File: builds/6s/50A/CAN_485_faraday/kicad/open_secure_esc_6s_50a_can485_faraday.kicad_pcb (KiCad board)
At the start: 4 copper layers, 32 x 66.1 mm, 59 parts, among them J1 SolderPad_1x04_SMD_P1.27mm_Pr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, J2 SolderPad_1x02_SMD_P2.54mm, J3 SolderPad_1x02_SMD_P2.54mm, J4A SolderWirePad_1x01_SMD_5x10mm, J4B SolderWirePad_1x01_SMD_5x10mm, J4C SolderWirePad_1x01_SMD_5x10mm, J5A SolderWire-6sqmm_1x01_D3.5mm_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, J5B SolderWire-6sqmm_1x01_D3.5mm_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, Q1 Toshiba_2-5W1A_SOP-Advance-N_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, Q2 Toshiba_2-5W1A_SOP-Advance-N_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, Q3 Toshiba_2-5W1A_SOP-Advance-N_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, Q4 Toshiba_2-5W1A_SOP-Advance-N_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, Q5 Toshiba_2-5W1A_SOP-Advance-N_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, Q6 Toshiba_2-5W1A_SOP-Advance-N_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, U1 LQFP-64_10x10mm_P0.5mm, U2 Infineon_PG-USON-10-2-4_3x3mm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, U3 SOIC-20W_7.5x12.8mm_P1.27mm, U4 SOIC-20W_7.5x12.8mm_P1.27mm, U5 TI_RTA0040B_WQFN-40_6x6mm_P0.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, U6 SOIC-8_3.9x4.9mm_P1.27mm, U7 SOIC-8_3.9x4.9mm_P1.27mm, U8 SOIC-8_3.9x4.9mm_P1.27mm

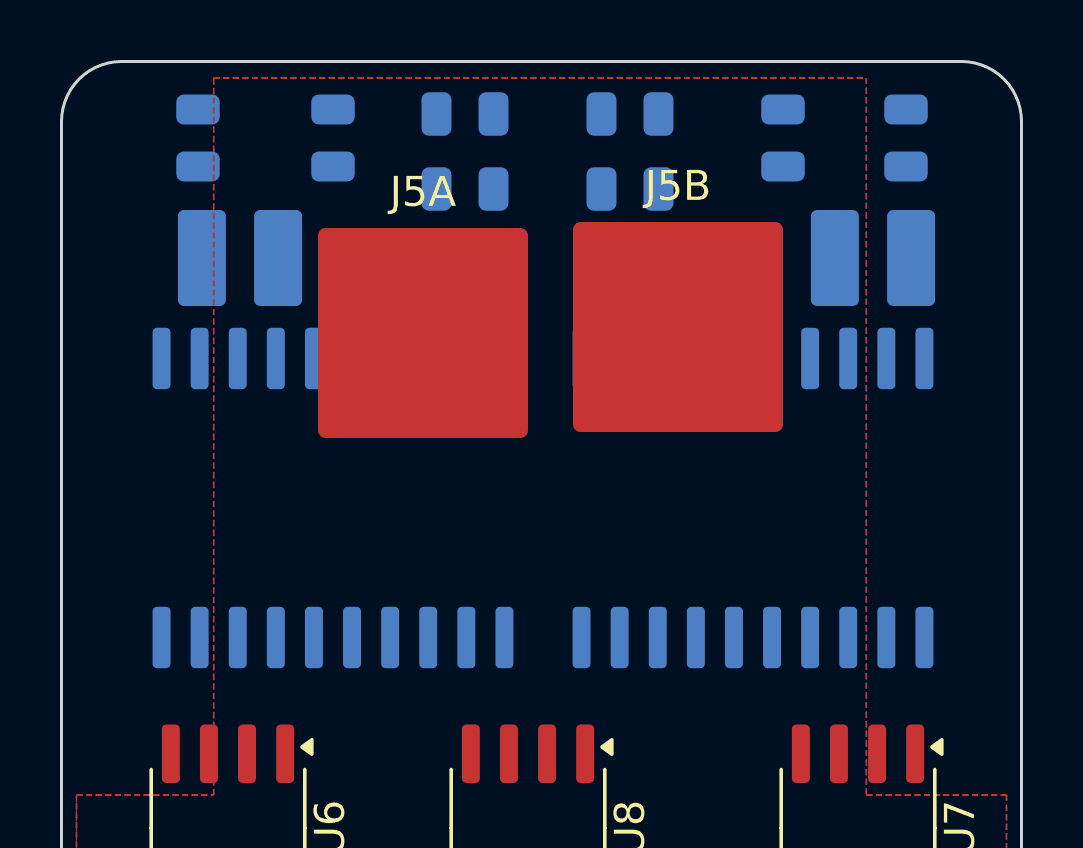
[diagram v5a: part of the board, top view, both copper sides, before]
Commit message: Creepage 7.51 -> 7.98 mm: the ceiling was my formula, not the board
The repo owner pushed back on two assertions and both were wrong.

FIRST: I claimed the FET columns could not move inboard because SH1's land is
a fixed 22.20 mm and they must sit within it. They already overhang it --
Q1/Q2 by 0.75 mm, Q5/Q6 by 2.75 mm -- with 5.30 and 6.30 mm of slack between
columns. The claim was asserted without checking.

SECOND, AND THE REAL ONE: edge_path() computed insetA + thickness + insetB,
which silently assumes two opposite-face parts sit at the same position ALONG
the edge. They rarely do. The true creepage path is the unfolded surface
distance,

    sqrt( along_edge_separation^2 + (insetA + thickness + insetB)^2 )

U3 against Q2 are ~26 mm apart in y, so the real path is 27.15 mm where the
harness was reporting 7.83. Every opposite-face pair was being scored as
though it sat directly across the edge.

With that corrected the picture inverts. The FETs stop being binders
entirely -- every around-edge pair is 7.98 mm or better -- and the only real
constraint is the in-plane U3.20 <-> U4.10 pair, which is exactly what
spreading the transceivers apart relieves. Sweeping it:

    spread +/-0.0  creepage 7.51  DRC 0
    spread +/-0.5  creepage 7.83  DRC 0
    spread +/-1.0  creepage 7.98  DRC 0   <- applied
    spread +/-2.0  creepage 7.98  DRC 0
    spread +/-2.5  creepage 7.98  DRC 4

Applied +/-1.0 mm. Creepage 7.98 with 0.48 mm of margin instead of 0.01,
DRC electrical 0, isolated lead unchanged at 9.76 mm, both isolation rules
still passing. No board resize needed.

This is the third harness bug found by checking it against geometry rather
than trusting its output -- after measuring pad centres instead of edges, and
omitting the around-edge path entirely. Each was caught by a result that did
not match the drawing, which is the argument for keeping the harness cheap to
re-derive from first principles.

12.5.al is corrected in place: it previously recorded 7.51 mm as a s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
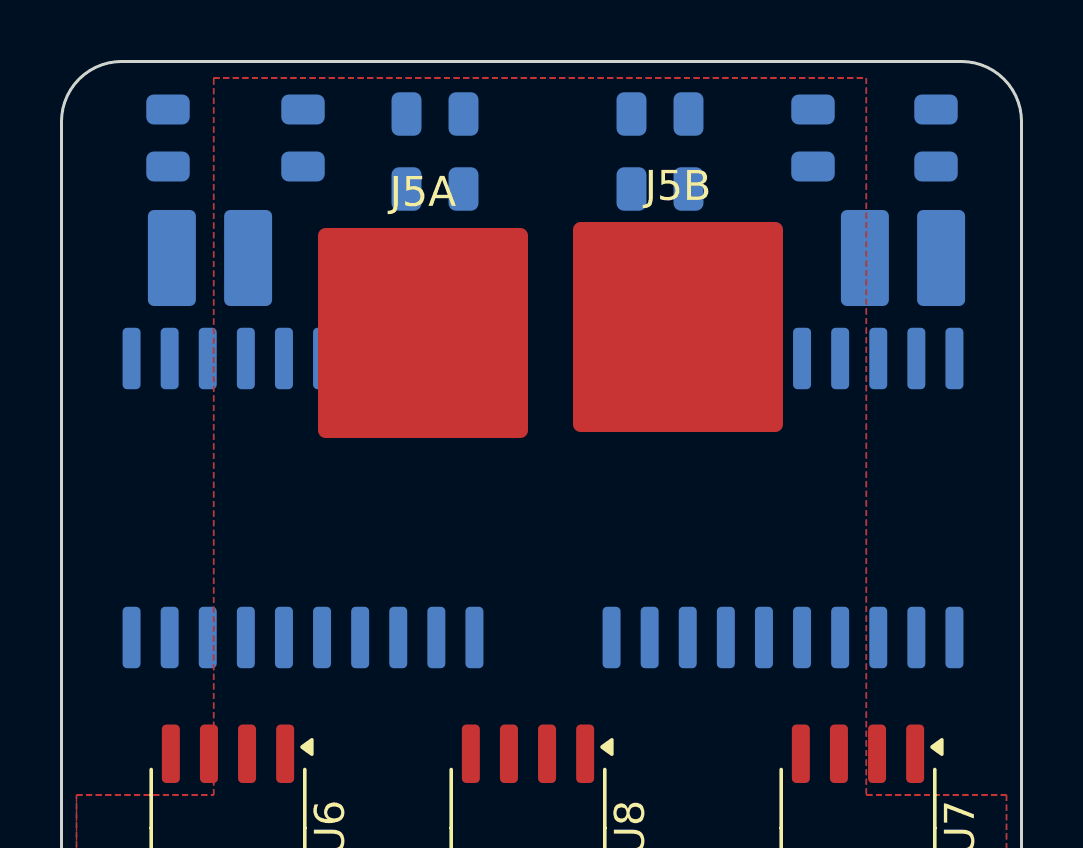
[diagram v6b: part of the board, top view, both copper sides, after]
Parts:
- moved C11 1.00 mm to (32.4, 21.7)
- moved C12 1.00 mm to (32.4, 24.2)
- moved C13 1.00 mm to (28.0, 22.5)
- moved C14 1.00 mm to (23.5, 22.5)
- moved C15 1.00 mm to (39.9, 21.7)
- moved C16 1.00 mm to (39.9, 24.2)
- moved C17 1.00 mm to (45.0, 22.5)
- moved C18 1.00 mm to (49.1, 22.5)
- moved FB1 1.00 mm to (31.9, 26.5)
- moved FB2 1.00 mm to (29.4, 26.5)
- moved FB3 1.00 mm to (39.9, 26.5)
- moved FB4 1.00 mm to (42.4, 26.5)
- moved J2 1.00 mm to (24.9, 26.5)
- moved J3 1.00 mm to (48.0, 26.5)
- moved U3 1.00 mm to (28.0, 34.5)
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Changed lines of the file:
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@@
 	(footprint "C_0805_2012Metric"
 		(layer "B.Cu")
-		(at 29 22.5 -90)
+		(at 28 22.5 -90)
 		(descr "Capacitor SMD 0805 (2012 Metric), square (rectangular) end terminal, IPC-7351 nominal, (Body size source: IPC-SM-782 page 76, https://www.pcb-3d.com/wordpress/wp-content/uploads/ipc-sm-782a_amendment_1_and_2.pdf, https://docs.google.com/spreadsheets/d/1BsfQQcO9C6DZCsRaXUlFlo91Tg2WpOkGARC1WS5S8t0/edit?usp=sharing), generated with kicad-footprint-generator")
 		(tags "capacitor")
@@
 	(footprint "C_0805_2012Metric"
 		(layer "B.Cu")
-		(at 33.4 21.7)
+		(at 32.4 21.7)
 		(descr "Capacitor SMD 0805 (2012 Metric), square (rectangular) end terminal, IPC-7351 nominal, (Body size source: IPC-SM-782 page 76, https://www.pcb-3d.com/wordpress/wp-content/uploads/ipc-sm-782a_amendment_1_and_2.pdf, https://docs.google.com/spreadsheets/d/1BsfQQcO9C6DZCsRaXUlFlo91Tg2WpOkGARC1WS5S8t0/edit?usp=sharing), generated with kicad-footprint-generator")
 		(tags "capacitor")
@@
 	(footprint "L_0402_1005Metric"
 		(layer "B.Cu")
-		(at 38.9 26.5)
+		(at 39.9 26.5)
 		(descr "Inductor SMD 0402 (1005 Metric), square (rectangular) end terminal, IPC-7351 nominal, (Body size source: http://www.tortai-tech.com/upload/download/2011102023233369053.pdf), generated with kicad-footprint-generator")
 		(tags "inductor")
@@
 	(footprint "SolderPad_1x02_SMD_P2.54mm"
 		(layer "B.Cu")
-		(at 25.9 26.5)
+		(at 24.9 26.5)
 		(descr "Bare SMD solder-pad strip, 2 pads, 2.54 mm pitch, 1.6 x 3.2 mm pads. Replaces a through-hole pin header so the opposite board side stays usable -- see symbols/tools/gen_smd_solder_pad_footprints.py. No connector body, no retention, no mating part: a wire solders directly to the pad. Pad geometry is an ENGINEERING DEFAULT (AGENTS.md Sec.4), not a datasheet or IPC value. Precedent: Vimdrones ESC S50 [47] 'CAN Port Connector: Solder PAD'.")
 		(tags "solder pad SMD wire connector 1x02 2.54mm")
@@
 	(footprint "SOIC-20W_7.5x12.8mm_P1.27mm"
 		(layer "B.Cu")
-		(at 43 34.5 90)
+		(at 44 34.5 90)
 		(descr "SOIC, 20 Pin (JEDEC MS-013AC, https://www.analog.com/media/en/package-pcb-resources/package/233848rw_20.pdf), generated with kicad-footprint-generator ipc_gullwing_generator.py")
 		(tags "SOIC SO")
@@
 	(footprint "C_0805_2012Metric"
 		(layer "B.Cu")
-		(at 38.9 21.7)
+		(at 39.9 21.7)
 		(descr "Capacitor SMD 0805 (2012 Metric), square (rectangular) end terminal, IPC-7351 nominal, (Body size source: IPC-SM-782 page 76, https://www.pcb-3d.com/wordpress/wp-content/uploads/ipc-sm-782a_amendment_1_and_2.pdf, https://docs.google.com/spreadsheets/d/1BsfQQcO9C6DZCsRaXUlFlo91Tg2WpOkGARC1WS5S8t0/edit?usp=sharing), generated with kicad-footprint-generator")
 		(tags "capacitor")
@@
 	(footprint "SOIC-20W_7.5x12.8mm_P1.27mm"
 		(layer "B.Cu")
-		(at 29 34.5 90)
+		(at 28 34.5 90)
 		(descr "SOIC, 20 Pin (JEDEC MS-013AC, https://www.analog.com/media/en/package-pcb-resources/package/233848rw_20.pdf), generated with kicad-footprint-generator ipc_gullwing_generator.py")
 		(tags "SOIC SO")
@@
 	(footprint "C_0805_2012Metric"
 		(layer "B.Cu")
-		(at 44 22.5 -90)
+		(at 45 22.5 -90)
 		(descr "Capacitor SMD 0805 (2012 Metric), square (rectangular) end terminal, IPC-7351 nominal, (Body size source: IPC-SM-782 page 76, https://www.pcb-3d.com/wordpress/wp-content/uploads/ipc-sm-782a_amendment_1_and_2.pdf, https://docs.google.com/spreadsheets/d/1BsfQQcO9C6DZCsRaXUlFlo91Tg2WpOkGARC1WS5S8t0/edit?usp=sharing), generated with kicad-footprint-generator")
 		(tags "capacitor")
@@
 	(footprint "L_0402_1005Metric"
 		(layer "B.Cu")
-		(at 30.4 26.5)
+		(at 29.4 26.5)
 		(descr "Inductor SMD 0402 (1005 Metric), square (rectangular) end terminal, IPC-7351 nominal, (Body size source: http://www.tortai-tech.com/upload/download/2011102023233369053.pdf), generated with kicad-footprint-generator")
 		(tags "inductor")
@@
 	(footprint "C_0805_2012Metric"
 		(layer "B.Cu")
-		(at 33.4 24.2)
+		(at 32.4 24.2)
 		(descr "Capacitor SMD 0805 (2012 Metric), square (rectangular) end terminal, IPC-7351 nominal, (Body size source: IPC-SM-782 page 76, https://www.pcb-3d.com/wordpress/wp-content/uploads/ipc-sm-782a_amendment_1_and_2.pdf, https://docs.google.com/spreadsheets/d/1BsfQQcO9C6DZCsRaXUlFlo91Tg2WpOkGARC1WS5S8t0/edit?usp=sharing), generated with kicad-footprint-generator")
 		(tags "capacitor")
@@
 	(footprint "L_0402_1005Metric"
 		(layer "B.Cu")
-		(at 41.4 26.5)
+		(at 42.4 26.5)
 		(descr "Inductor SMD 0402 (1005 Metric), square (rectangular) end terminal, IPC-7351 nominal, (Body size source: http://www.tortai-tech.com/upload/download/2011102023233369053.pdf), generated with kicad-footprint-generator")
 		(tags "inductor")
@@
 	(footprint "C_0805_2012Metric"
 		(layer "B.Cu")
-		(at 24.5 22.5 -90)
+		(at 23.5 22.5 -90)
 		(descr "Capacitor SMD 0805 (2012 Metric), square (rectangular) end terminal, IPC-7351 nominal, (Body size source: IPC-SM-782 page 76, https://www.pcb-3d.com/wordpress/wp-content/uploads/ipc-sm-782a_amendment_1_and_2.pdf, https://docs.google.com/spreadsheets/d/1BsfQQcO9C6DZCsRaXUlFlo91Tg2WpOkGARC1WS5S8t0/edit?usp=sharing), generated with kicad-footprint-generator")
 		(tags "capacitor")
@@
 	(footprint "L_0402_1005Metric"
 		(layer "B.Cu")
-		(at 32.9 26.5)
+		(at 31.9 26.5)
 		(descr "Inductor SMD 0402 (1005 Metric), square (rectangular) end terminal, IPC-7351 nominal, (Body size source: http://www.tortai-tech.com/upload/download/2011102023233369053.pdf), generated with kicad-footprint-generator")
 		(tags "inductor")
@@
 	(footprint "SolderPad_1x02_SMD_P2.54mm"
 		(layer "B.Cu")
-		(at 47 26.5)
+		(at 48 26.5)
 		(descr "Bare SMD solder-pad strip, 2 pads, 2.54 mm pitch, 1.6 x 3.2 mm pads. Replaces a through-hole pin header so the opposite board side stays usable -- see symbols/tools/gen_smd_solder_pad_footprints.py. No connector body, no retention, no mating part: a wire solders directly to the pad. Pad geometry is an ENGINEERING DEFAULT (AGENTS.md Sec.4), not a datasheet or IPC value. Precedent: Vimdrones ESC S50 [47] 'CAN Port Connector: Solder PAD'.")
 		(tags "solder pad SMD wire connector 1x02 2.54mm")
@@
 	(footprint "C_0805_2012Metric"
 		(layer "B.Cu")
-		(at 38.9 24.2)
+		(at 39.9 24.2)
 		(descr "Capacitor SMD 0805 (2012 Metric), square (rectangular) end terminal, IPC-7351 nominal, (Body size source: IPC-SM-782 page 76, https://www.pcb-3d.com/wordpress/wp-content/uploads/ipc-sm-782a_amendment_1_and_2.pdf, https://docs.google.com/spreadsheets/d/1BsfQQcO9C6DZCsRaXUlFlo91Tg2WpOkGARC1WS5S8t0/edit?usp=sharing), generated with kicad-footprint-generator")
 		(tags "capacitor")
@@
 	(footprint "C_0805_2012Metric"
 		(layer "B.Cu")
-		(at 48.1 22.5 -90)
+		(at 49.1 22.5 -90)
 		(descr "Capacitor SMD 0805 (2012 Metric), square (rectangular) end terminal, IPC-7351 nominal, (Body size source: IPC-SM-782 page 76, https://www.pcb-3d.com/wordpress/wp-content/uploads/ipc-sm-782a_amendment_1_and_2.pdf, https://docs.google.com/spreadsheets/d/1BsfQQcO9C6DZCsRaXUlFlo91Tg2WpOkGARC1WS5S8t0/edit?usp=sharing), generated with kicad-footprint-generator")
 		(tags "capacitor")
